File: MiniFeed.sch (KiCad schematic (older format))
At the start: 64 parts, among them J1 Connector_1, J2 Uart, J3 Debug, J4 Connector_2, M1 Motor_DC, SW1 SW_-, SW2 SW_S, SW3 SW_+, SW4 Detect1, SW5 Detect2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

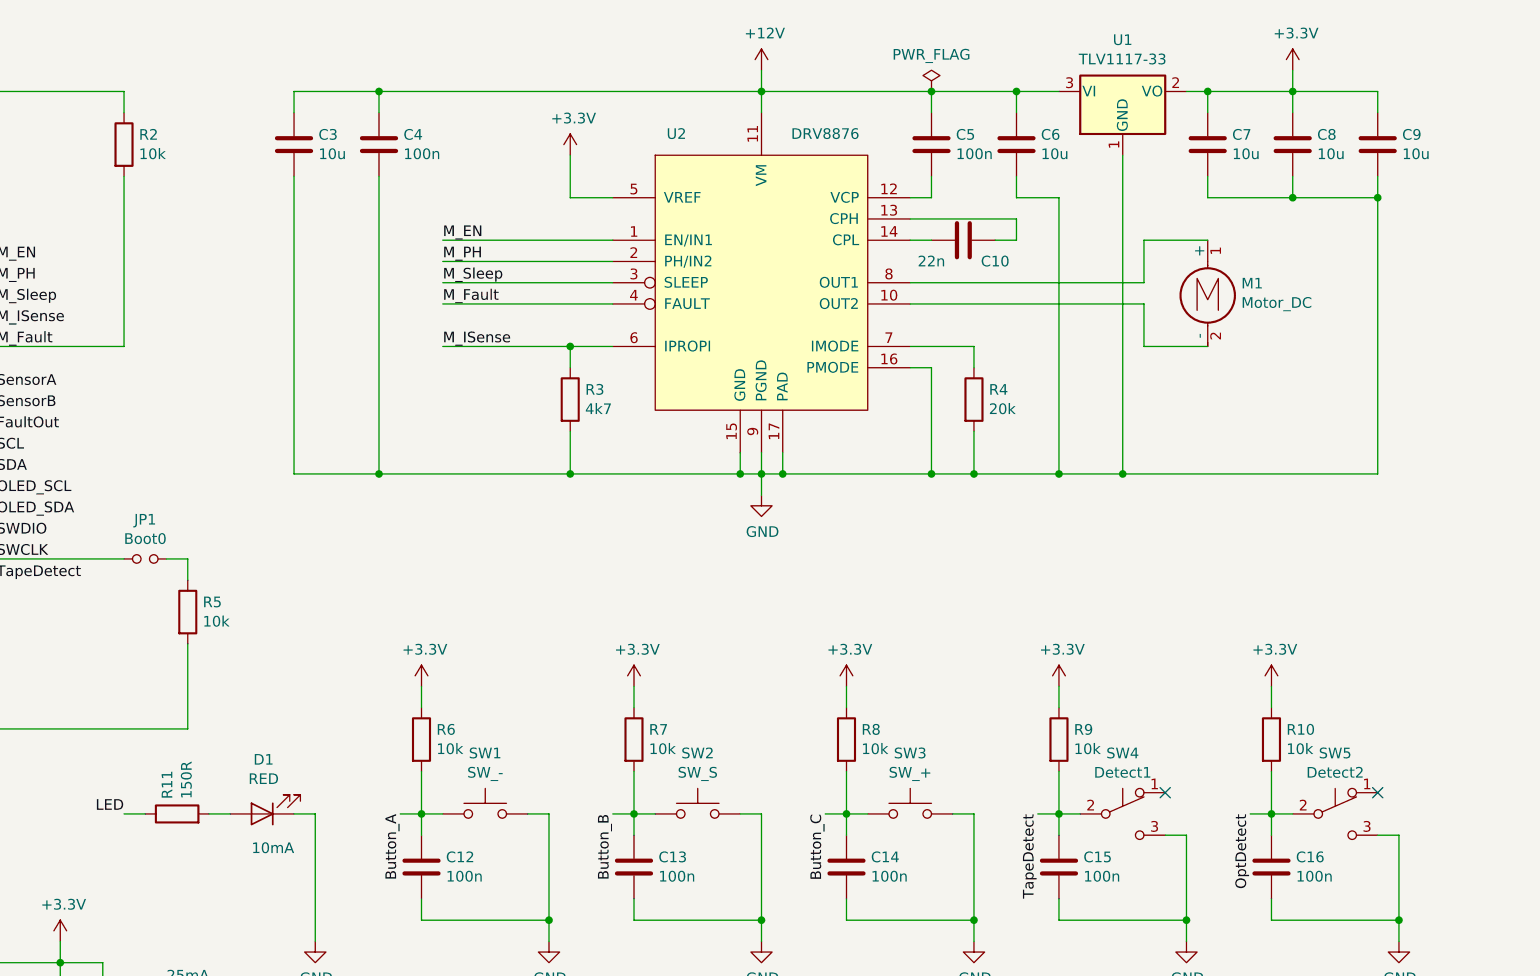
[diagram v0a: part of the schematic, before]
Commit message: Fixed LDO design: Added resistor to increase ESR for LDO. Added diode to LDO to protect the regulator if the input instantaneously is shorted to GND.
Fixed the SCL trace.
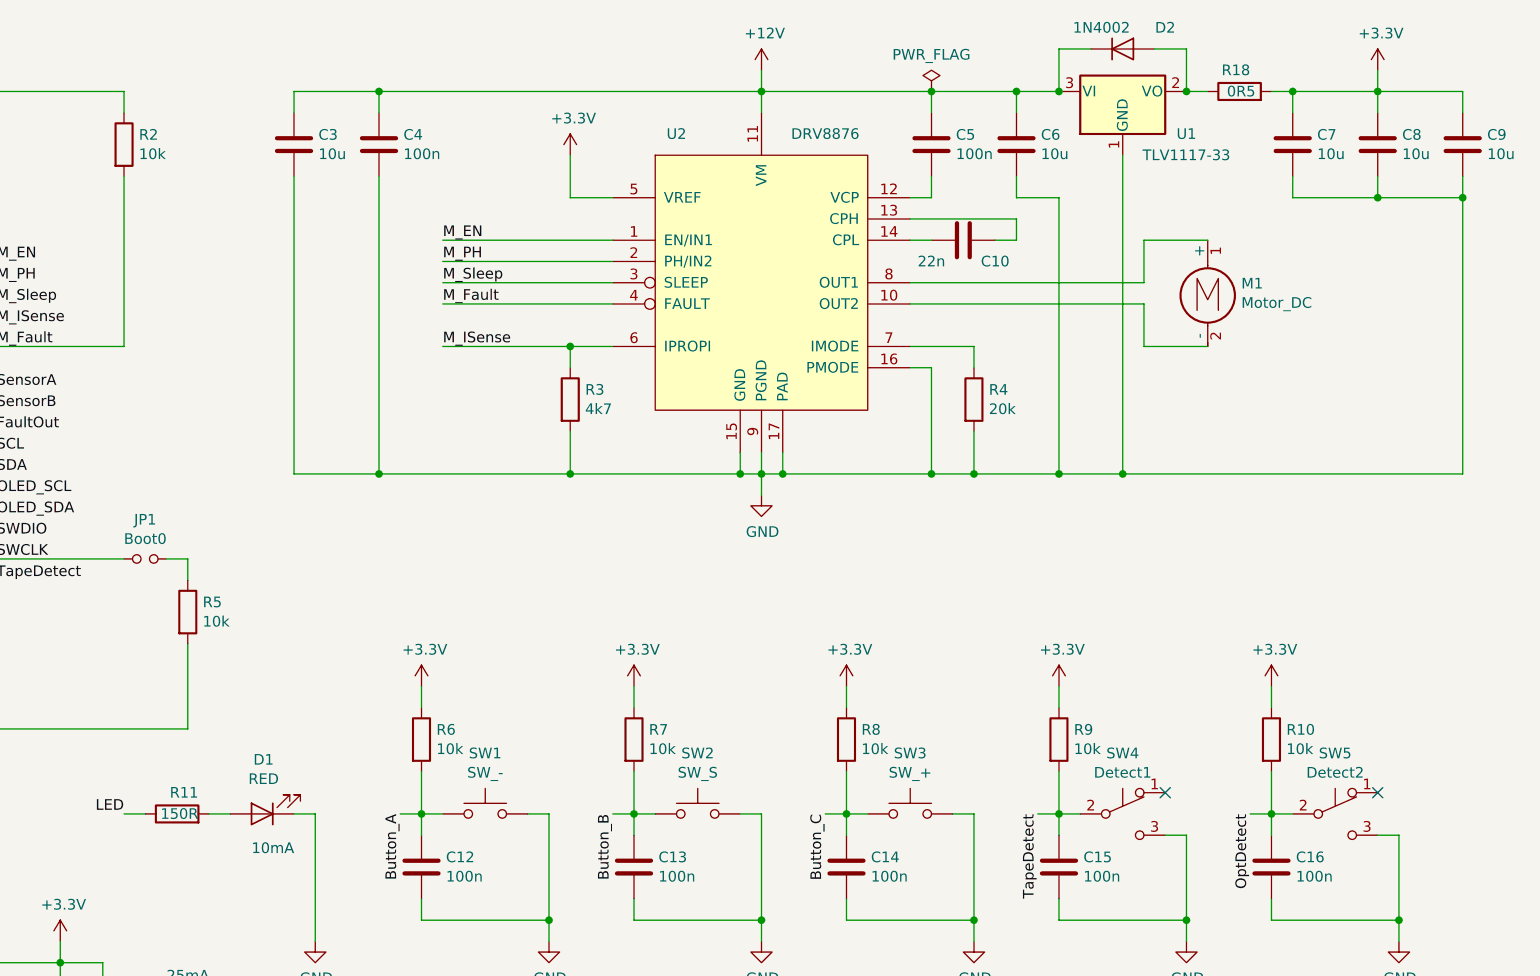
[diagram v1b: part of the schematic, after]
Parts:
- added D2: 1N4002, Diode_SMD:D_SOD-123F, symbol Device:D
- added R18: 0R5, Resistor_SMD:R_0805_2012Metric, symbol Device:R
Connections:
- net +12V: now also D2.1 (K)
- net +3V3: now also R18.2; no longer U1.2 (VO)
- new net: D2.2 (A), R18.1, U1.2 (VO)
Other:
- moved on the sheet: C7, C8, C9
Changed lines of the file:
@@
 Sheet 1 1
 Title "MiniFeed"
-Date "2020-11-15"
-Rev "0.1"
+Date "2020-12-17"
+Rev "0.2"
 Comp "SG-O"
 Comment1 "©CC BY 4.0"
@@
 U 1 1 5FA649AD
 P 9300 900
-F 0 "U1" H 9300 1142 50  0000 C CNN
-F 1 "TLV1117-33" H 9300 1051 50  0000 C CNN
+F 0 "U1" H 9600 700 50  0000 C CNN
+F 1 "TLV1117-33" H 9600 600 50  0000 C CNN
 F 2 "Package_TO_SOT_SMD:SOT-223-3_TabPin2" H 9300 900 50  0001 C CNN
 F 3 "http://www.ti.com/lit/ds/symlink/tlv1117.pdf" H 9300 900 50  0001 C CNN
@@
 L Device:C C7
 U 1 1 5FAAD39F
-P 9700 1150
-F 0 "C7" H 9815 1196 50  0000 L CNN
-F 1 "10u" H 9815 1105 50  0000 L CNN
-F 2 "Capacitor_SMD:C_1206_3216Metric" H 9738 1000 50  0001 C CNN
-F 3 "~" H 9700 1150 50  0001 C CNN
-F 4 "C14860" H 9700 1150 50  0001 C CNN "lcsc#"
-F 5 "CL31B106KAHNNNE" H 9700 1150 50  0001 C CNN "manf#"
-	1    9700 1150
-	1    0    0    -1
-$EndComp
-$Comp
-L Device:C C8
-U 1 1 5FAB7CB8
 P 10100 1150
-F 0 "C8" H 10215 1196 50  0000 L CNN
+F 0 "C7" H 10215 1196 50  0000 L CNN
 F 1 "10u" H 10215 1105 50  0000 L CNN
 F 2 "Capacitor_SMD:C_1206_3216Metric" H 10138 1000 50  0001 C CNN
@@
 $EndComp
 $Comp
-L Device:C C9
-U 1 1 5FAD3113
+L Device:C C8
+U 1 1 5FAB7CB8
 P 10500 1150
-F 0 "C9" H 10615 1196 50  0000 L CNN
+F 0 "C8" H 10615 1196 50  0000 L CNN
 F 1 "10u" H 10615 1105 50  0000 L CNN
 F 2 "Capacitor_SMD:C_1206_3216Metric" H 10538 1000 50  0001 C CNN
@@
 	1    0    0    -1
 $EndComp
-Wire Wire Line
-	9600 900  9700 900
-Wire Wire Line
-	10500 900  10500 1000
+$Comp
+L Device:C C9
+U 1 1 5FAD3113
+P 10900 1150
+F 0 "C9" H 11015 1196 50  0000 L CNN
+F 1 "10u" H 11015 1105 50  0000 L CNN
+F 2 "Capacitor_SMD:C_1206_3216Metric" H 10938 1000 50  0001 C CNN
+F 3 "~" H 10900 1150 50  0001 C CNN
+F 4 "C14860" H 10900 1150 50  0001 C CNN "lcsc#"
+F 5 "CL31B106KAHNNNE" H 10900 1150 50  0001 C CNN "manf#"
+	1    10900 1150
+	1    0    0    -1
+$EndComp
+Wire Wire Line
+	10900 900  10900 1000
+Wire Wire Line
+	10500 1000 10500 900
+Connection ~ 10500 900
+Wire Wire Line
+	10500 900  10900 900
 Wire Wire Line
 	10100 1000 10100 900
-Connection ~ 10100 900
 Wire Wire Line
 	10100 900  10500 900
 Wire Wire Line
-	9700 1000 9700 900
-Connection ~ 9700 900
-Wire Wire Line
-	9700 900  10100 900
-Wire Wire Line
 	9400 1900 9400 2100
 Wire Wire Line
 	9400 2100 9700 2100
 Wire Wire Line
-	9700 1300 9700 1400
-Wire Wire Line
-	9700 1400 10100 1400
-Wire Wire Line
-	10500 1400 10500 1300
-Wire Wire Line
 	10100 1300 10100 1400
-Connection ~ 10100 1400
 Wire Wire Line
 	10100 1400 10500 1400
 Wire Wire Line
-	9300 2700 10500 2700
-Wire Wire Line
-	10500 2700 10500 1400
+	10900 1400 10900 1300
+Wire Wire Line
+	10500 1300 10500 1400
+Connection ~ 10500 1400
+Wire Wire Line
+	10500 1400 10900 1400
+Wire Wire Line
+	10900 2700 10900 1400
 Connection ~ 9300 2700
-Connection ~ 10500 1400
-Wire Wire Line
-	10100 800  10100 900
+Connection ~ 10900 1400
+Wire Wire Line
+	10500 800  10500 900
 $Comp
 L power:+3.3V #PWR0123
@@
 L power:+3.3V #PWR0124
 U 1 1 5FB595F5
-P 10100 800
-F 0 "#PWR0124" H 10100 650 50  0001 C CNN
-F 1 "+3.3V" H 10115 973 50  0000 C CNN
-F 2 "" H 10100 800 50  0001 C CNN
-F 3 "" H 10100 800 50  0001 C CNN
-	1    10100 800
+P 10500 800
+F 0 "#PWR0124" H 10500 650 50  0001 C CNN
+F 1 "+3.3V" H 10515 973 50  0000 C CNN
+F 2 "" H 10500 800 50  0001 C CNN
+F 3 "" H 10500 800 50  0001 C CNN
+	1    10500 800
 	1    0    0    -1
 $EndComp
@@
 U 1 1 6001C827
 P 4850 4300
-F 0 "R11" H 4920 4346 50  0000 L CNN
-F 1 "150R" H 4920 4255 50  0000 L CNN
+F 0 "R11" V 4950 4200 50  0000 L CNN
+F 1 "150R" V 4850 4200 50  0000 L CNN
 F 2 "Resistor_SMD:R_0603_1608Metric" V 4780 4300 50  0001 C CNN
 F 3 "~" H 4850 4300 50  0001 C CNN
@@
 Wire Wire Line
 	8900 5600 9000 5600
+$Comp
+L Device:R R18
+U 1 1 5FC2F1D3
+P 9850 900
+F 0 "R18" V 9950 850 50  0000 L CNN
+F 1 "0R5" V 9850 825 50  0000 L CNN
+F 2 "Resistor_SMD:R_0805_2012Metric" V 9780 900 50  0001 C CNN
+F 3 "~" H 9850 900 50  0001 C CNN
+F 4 "C286632" H 9850 900 50  0001 C CNN "lcsc#"
+F 5 "RS-05MR50JT" H 9850 900 50  0001 C CNN "manf#"
+	1    9850 900
+	0    -1   -1   0
+$EndComp
+Wire Wire Line
+	9600 900  9700 900
+Wire Wire Line
+	9300 2700 10900 2700
+Wire Wire Line
+	10000 900  10100 900
+Connection ~ 10100 900
+$Comp
+L Device:D D2
+U 1 1 5FCF0EA8
+P 9300 700
+F 0 "D2" H 9500 800 50  0000 C CNN
+F 1 "1N4002" H 9200 800 50  0000 C CNN
+F 2 "Diode_SMD:D_SOD-123F" H 9300 700 50  0001 C CNN
+F 3 "~" H 9300 700 50  0001 C CNN
+F 4 "1N4002W" H 9300 700 50  0001 C CNN "manf#"
+F 5 "C169542" H 9300 700 50  0001 C CNN "lcsc#"
+	1    9300 700
+	1    0    0    -1
+$EndComp
+Wire Wire Line
+	9600 900  9600 700
+Wire Wire Line
+	9600 700  9450 700
+Connection ~ 9600 900
+Wire Wire Line
+	9150 700  9000 700
+Wire Wire Line
+	9000 700  9000 900
+Connection ~ 9000 900
 $EndSCHEMATC

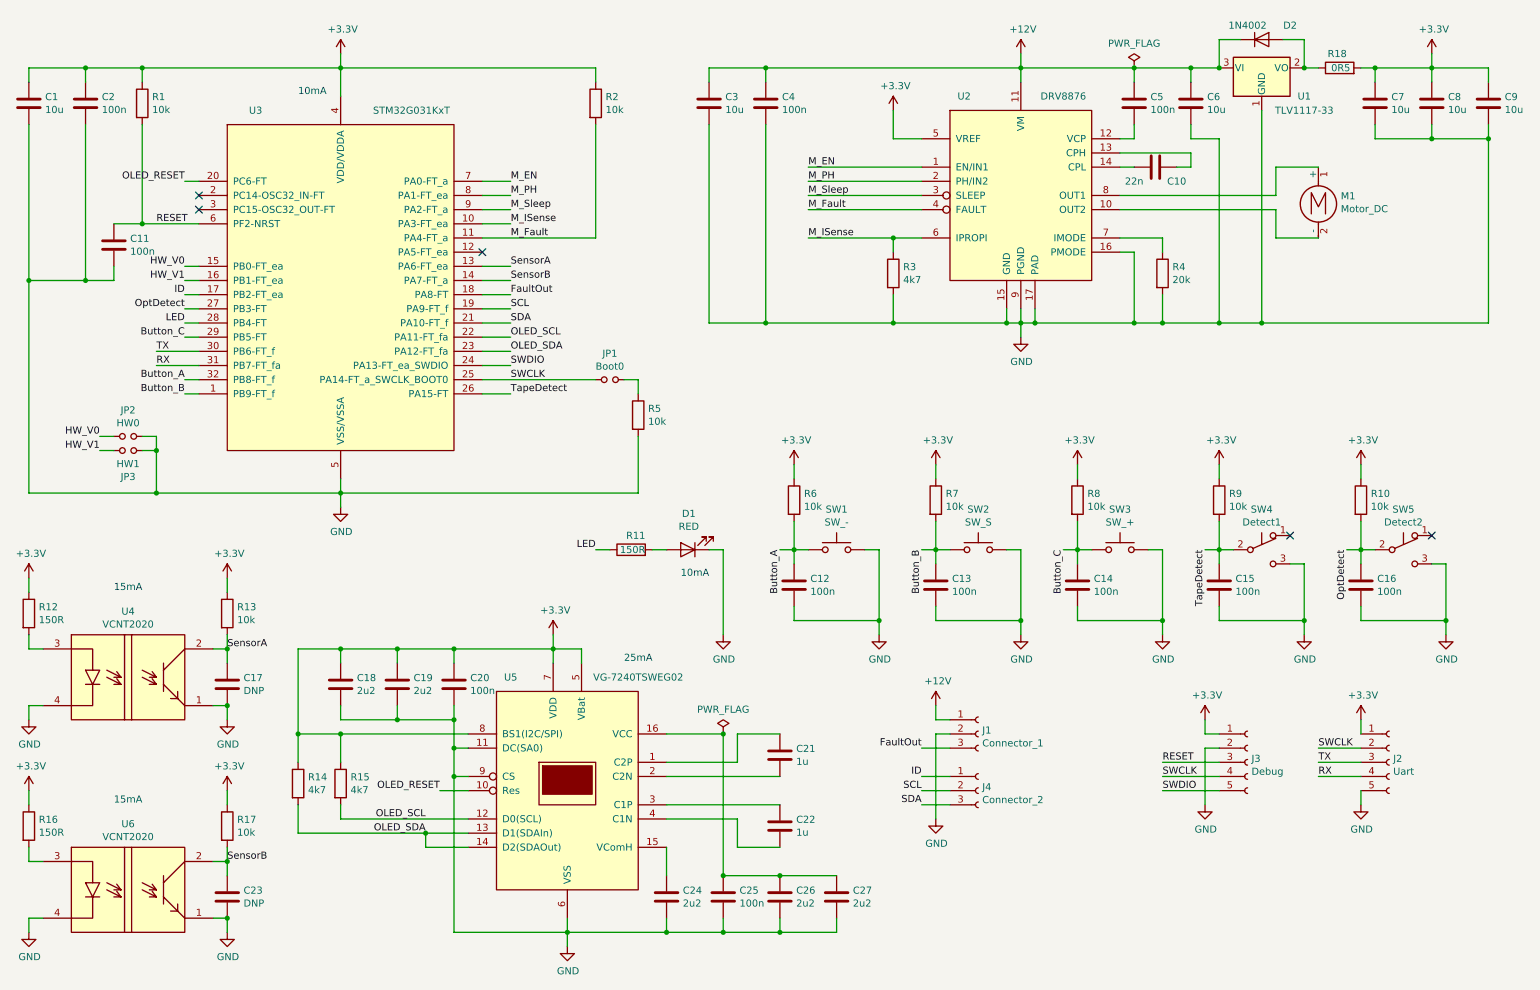
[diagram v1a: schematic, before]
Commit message: Removed voltage regulator Added input protection Added more VCNT2020 sensors Fixed the motor driver overcurrent protection Replaced push buttons with smaller models
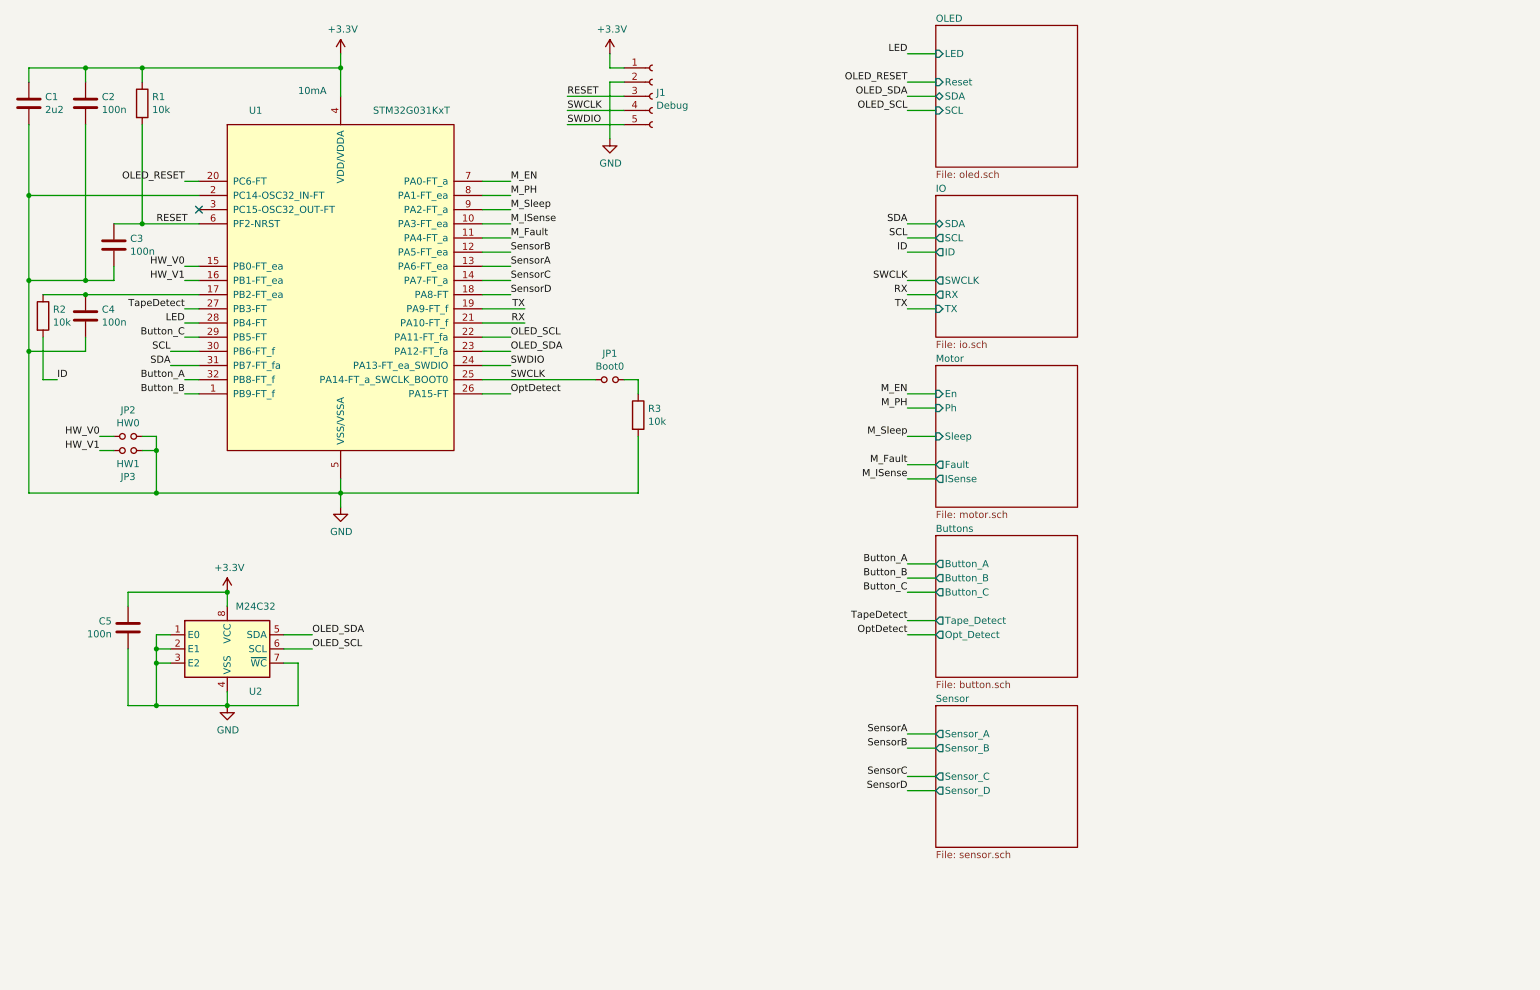
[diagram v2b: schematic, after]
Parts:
- removed C10: 22n, Capacitor_SMD:C_0603_1608Metric, symbol Device:C
- removed C12, C13, C14, C15, C16, C20, C25: 100n, Capacitor_SMD:C_0603_1608Metric, symbol Device:C
- removed C17, C23: DNP, Capacitor_SMD:C_0603_1608Metric, symbol Device:C
- removed C18, C19, C24, C26, C27: 2u2, Capacitor_SMD:C_0805_2012Metric, symbol Device:C
- removed C21, C22: 1u, Capacitor_SMD:C_0603_1608Metric, symbol Device:C
- removed C3, C6, C7, C8, C9: 10u, Capacitor_SMD:C_1206_3216Metric, symbol Device:C
- removed D1: RED, global:LED_0603_1608Metric_SIDE, symbol Device:LED
- removed D2: 1N4002, Diode_SMD:D_SOD-123F, symbol Device:D
- removed J1: Connector_1, global:PogoTarget_P2.5, symbol Connector:Conn_01x03_Female
- removed J2: Uart, Connector_PinSocket_2.54mm:PinSocket_1x05_P2.54mm_Vertical, symbol Connector:Conn_01x05_Female
- removed J4: Connector_2, global:PogoTarget_P2.5, symbol Connector:Conn_01x03_Female
- removed M1: Motor_DC, global:MotorN20, symbol Motor:Motor_DC
- removed R10, R13, R17, R6, R7, R8, R9: 10k, Resistor_SMD:R_0603_1608Metric, symbol Device:R
- removed R11, R12, R16: 150R, Resistor_SMD:R_0603_1608Metric, symbol Device:R
- removed R14, R15, R3: 4k7, Resistor_SMD:R_0603_1608Metric, symbol Device:R
- removed R18: 0R5, Resistor_SMD:R_0805_2012Metric, symbol Device:R
- removed R4: 20k, Resistor_SMD:R_0603_1608Metric, symbol Device:R
- removed SW1: SW_-, global:TS36CA-0.7, symbol Switch:SW_Push
- removed SW2: SW_S, global:TS36CA-0.7, symbol Switch:SW_Push
- removed SW3: SW_+, global:TS36CA-0.7, symbol Switch:SW_Push
- removed SW4: Detect1, global:MicroSwitchSMDLanding, symbol Switch:SW_Push_SPDT
- removed SW5: Detect2, global:MicroSwitchSMDLanding, symbol Switch:SW_Push_SPDT
- removed U1: TLV1117-33, Package_TO_SOT_SMD:SOT-223-3_TabPin2, symbol Regulator_Linear:TLV1117-33
- removed U2: DRV8876, Package_SO:HTSSOP-16-1EP_4.4x5mm_P0.65mm_EP3.4x5mm_Mask2.46x2.31mm_ThermalVias, symbol global:DRV8876
- removed U4, U6: VCNT2020, global:vcnt2020, symbol global:VCNT2020
- removed U5: VG-7240TSWEG02, global:VG-7240TSWEG02, symbol global:VG-7240TSWEG02
- added U2: M24C32, Package_SO:SOIC-8_3.9x4.9mm_P1.27mm, symbol Memory_EEPROM:M24C01-FMN
- C1: value 10u -> 2u2; footprint Capacitor_SMD:C_1206_3216Metric -> Capacitor_SMD:C_0805_2012Metric; lcsc# C14860 -> C19110; manf# CL31B106KAHNNNE -> CL21B225KAFNNNE
- renumbered C11 to C3, J3 to J1, R5 to R3, U3 to U1
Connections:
- net +3V3: now also C5.1, U2.8 (VCC); no longer R2.1
- net GND: now also C5.2, U1.2 (PC14-OSC32_IN-FT), U2.1 (E0), U2.2 (E1), U2.3 (E2), U2.4 (VSS), U2.7 (~WC)
- net ID: now also R2.2; no longer U1.17 (PB2-FT_ea)
- net M_Fault: no longer R2.2
- net OLED_SCL: now also U2.6 (SCL)
- net OLED_SDA: now also U2.5 (SDA)
- net OptDetect: now also U1.26 (PA15-FT); no longer U1.27 (PB3-FT)
- net RX: now also U1.21 (PA10-FT_f); no longer U1.31 (PB7-FT_fa)
- net SCL: now also U1.30 (PB6-FT_f); no longer U1.19 (PA9-FT_f)
- net SDA: now also U1.31 (PB7-FT_fa); no longer U1.21 (PA10-FT_f)
- net SensorB: now also U1.12 (PA5-FT_ea); no longer U1.14 (PA7-FT_a)
- net TX: now also U1.19 (PA9-FT_f); no longer U1.30 (PB6-FT_f)
- net TapeDetect: now also U1.27 (PB3-FT); no longer U1.26 (PA15-FT)
- net +12V: no longer names the net of C4.1
- net +12V: now also R2.1, U1.17 (PB2-FT_ea); no longer C5.1
- net FaultOut renamed SensorD
- new net SensorC: U1.14 (PA7-FT_a)
- no-connect marks 5 -> 1
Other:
- note removed: "15mA"
- note removed: "25mA"
- moved on the sheet: J1

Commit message: Added an optional power output header Changed the resistors for the VCNT2020 to improve performance
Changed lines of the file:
@@
 Sheet 1 6
 Title "MiniFeed"
-Date "2021-01-31"
+Date "2021-02-25"
 Rev "1.0"
 Comp "SG-O"
@@
 Wire Wire Line
 	600  1800 600  1300
+Wire Notes Line
+	1850 1750 1850 1850
+Wire Notes Line
+	1850 1850 1750 1850
+Wire Notes Line
+	1750 1850 1750 1750
+Wire Notes Line
+	1750 1750 1850 1750
+Wire Notes Line
+	1750 2850 1850 2850
+Wire Notes Line
+	1850 2850 1850 3050
+Wire Notes Line
+	1850 3050 1750 3050
+Wire Notes Line
+	1750 2850 1750 3050
+Wire Notes Line
+	1750 2550 1850 2550
+Wire Notes Line
+	1850 2550 1850 2650
+Wire Notes Line
+	1850 2650 1750 2650
+Wire Notes Line
+	1750 2650 1750 2550
+Wire Notes Line
+	3750 2150 3850 2150
+Wire Notes Line
+	3850 2150 3850 2250
+Wire Notes Line
+	3850 2250 3750 2250
+Wire Notes Line
+	3750 2250 3750 2150
+Wire Notes Line
+	3750 2450 3850 2450
+Wire Notes Line
+	3850 2550 3750 2550
+Wire Notes Line
+	3850 2750 3750 2750
+Wire Notes Line
+	3850 2450 3850 2750
+Wire Notes Line
+	3750 2450 3750 2750
+Wire Notes Line
+	3750 3150 3850 3150
+Wire Notes Line
+	3850 3150 3850 3250
+Wire Notes Line
+	3850 3250 3750 3250
+Wire Notes Line
+	3750 3250 3750 3150
 $EndSCHEMATC
